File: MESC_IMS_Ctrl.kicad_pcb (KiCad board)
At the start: 4 copper layers, 100 x 75 mm, 187 parts, among them J1 Conn_01x08_Female, J10 Conn_01x04_Male, J2 Conn_01x08_Female, J3 Conn_01x08_Female, J4 Conn_01x06_Male, J5 Conn_ARM_JTAG_SWD_10, J6 USB_C_Receptacle_USB2.0, J7 Conn_01x03_Male, J8 Conn_01x04_Male, J9 Conn_01x08_Male, U1 STM32F303CBTx, U2 LM5017MR, U3 TPS76333, U4 INA240A1PW, U5 UCC21520DW, U6 INA240A1PW, U7 UCC21520DW, U8 INA240A1PW, U9 UCC21520DW, Y1 ASE-8.000MHZ-LC-T

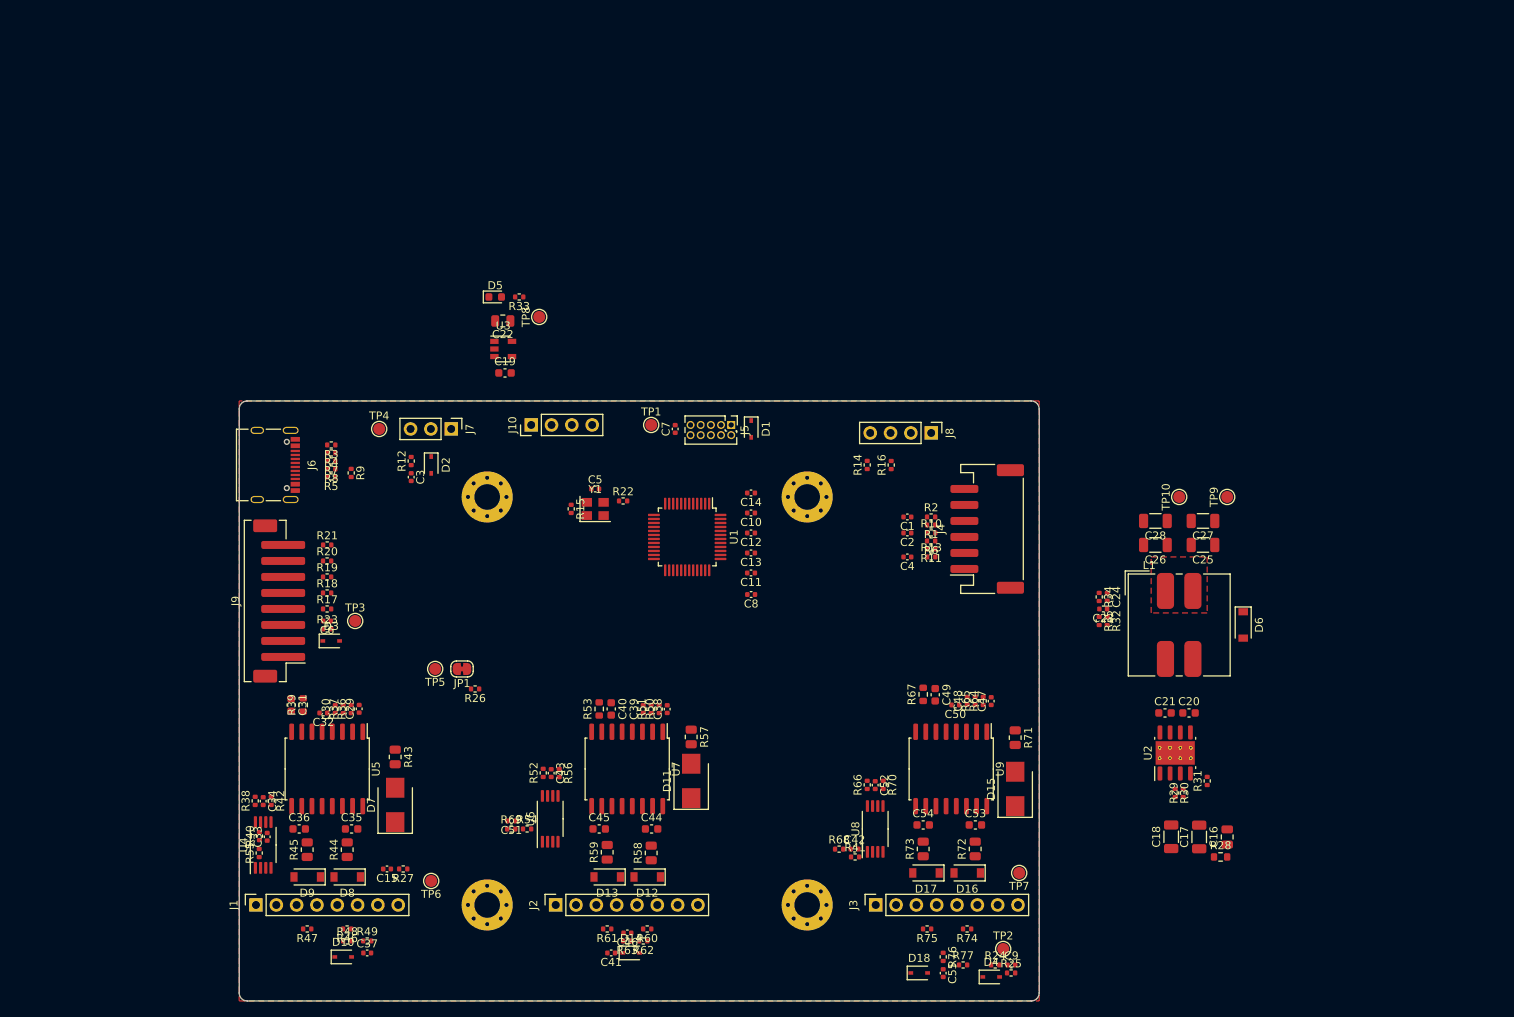
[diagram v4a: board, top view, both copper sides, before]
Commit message: Adding some basic test tracks
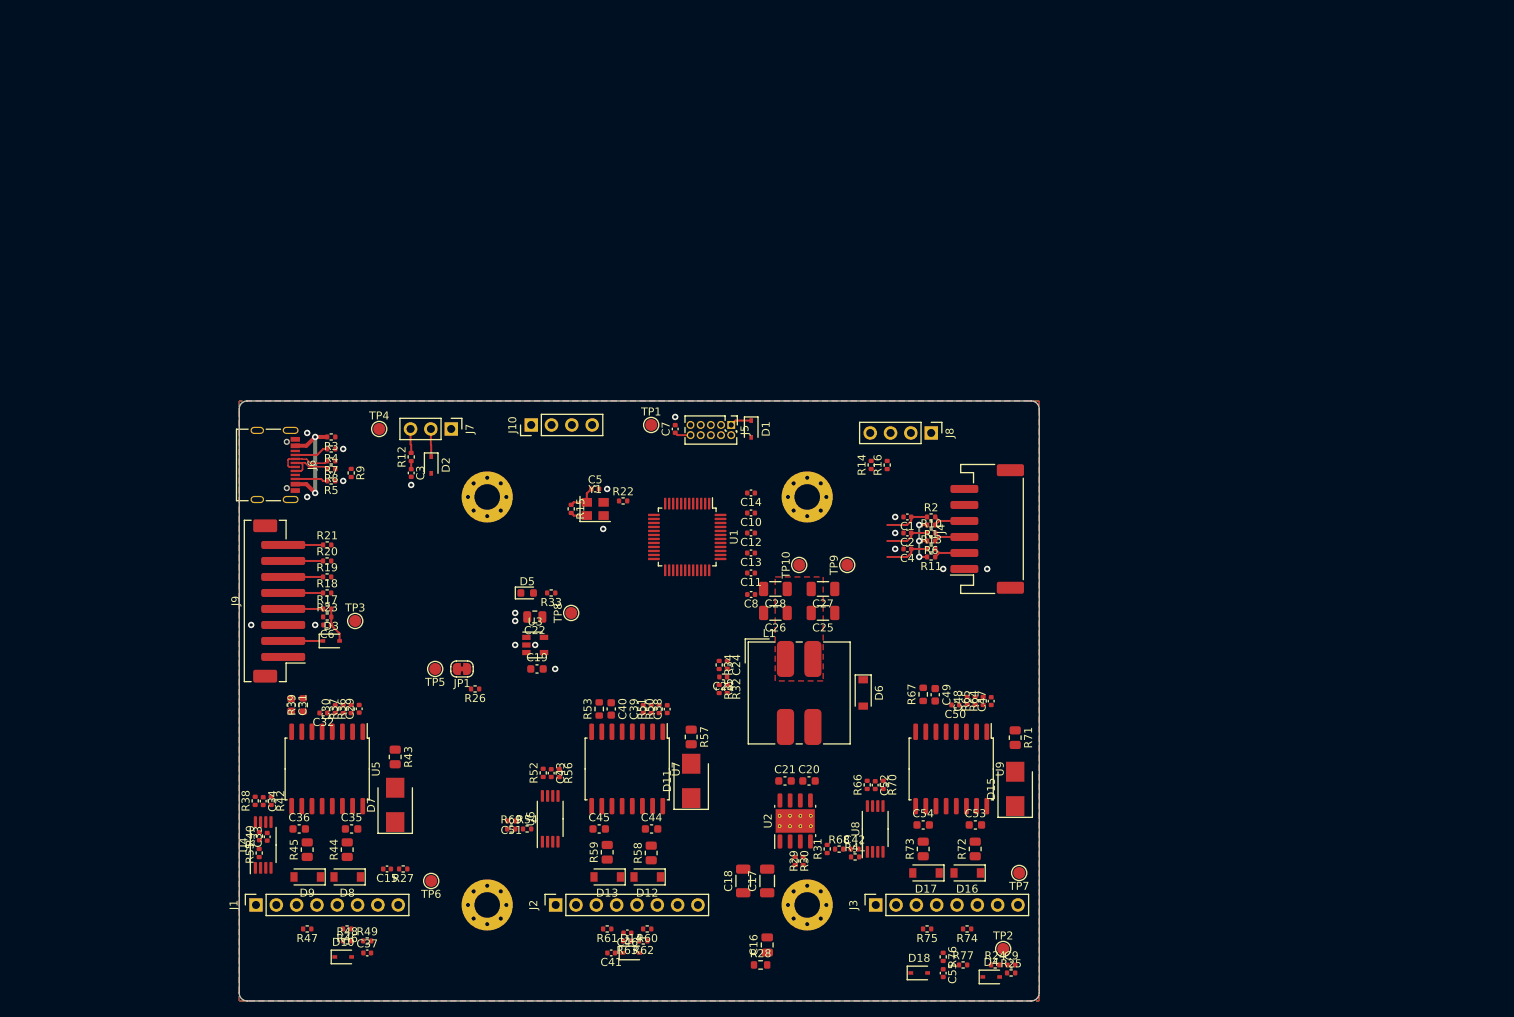
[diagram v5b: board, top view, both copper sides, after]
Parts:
- H1, H2, H3, H4: moved to F.Cu
- moved C16 59.1 mm to (175.0, 143.0)
- moved R28 59.1 mm to (174.2, 145.5)
- moved C17 54.3 mm to (175.0, 135.0)
- moved C18 53.8 mm to (172.0, 135.0)
- moved C20 48.3 mm to (180.2, 122.5)
- moved C21 48.3 mm to (177.2, 122.5)
- moved C23 48.3 mm to (169.5, 109.5)
- moved C24 48.3 mm to (170.0, 108.0)
- moved C25 48.3 mm to (182.0, 101.5)
- moved C26 48.3 mm to (176.0, 101.5)
- moved C27 48.3 mm to (182.0, 98.5)
- moved C28 48.3 mm to (176.0, 98.5)
- moved D6 48.3 mm to (187.0, 111.5)
- moved L1 48.3 mm to (179.0, 111.5)
- moved R29 48.3 mm to (179.5, 132.5)
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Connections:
- net Net-(J6-PadA6) renamed /D+
- net Net-(J6-PadA7) renamed /D-
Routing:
- net +3V3: track 0.00 -> 15.9 mm, vias 0 -> 3
- net Net-(J6-PadA4): track 0.00 -> 14.4 mm, vias 0 -> 2
- net /D-: track 0.00 -> 6.98 mm
- net /D+: track 0.00 -> 6.19 mm
- net /HALL_3: track 0.00 -> 5.70 mm
- net /HALL_2: track 0.00 -> 5.70 mm
- net /HALL_1: track 0.00 -> 5.69 mm
- net Net-(J9-Pad8): track 0.00 -> 4.99 mm
- net Net-(J9-Pad4): track 0.00 -> 4.99 mm
- net Net-(J9-Pad7): track 0.00 -> 4.98 mm
- net Net-(J9-Pad6): track 0.00 -> 4.98 mm
- net Net-(J9-Pad5): track 0.00 -> 4.98 mm
- net Net-(J4-Pad4): track 0.00 -> 4.56 mm
- net Net-(J4-Pad3): track 0.00 -> 4.56 mm
- net Net-(J4-Pad2): track 0.00 -> 4.56 mm
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- added copper zone on B.Cu, net GND
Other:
- copper layers 4 -> 2

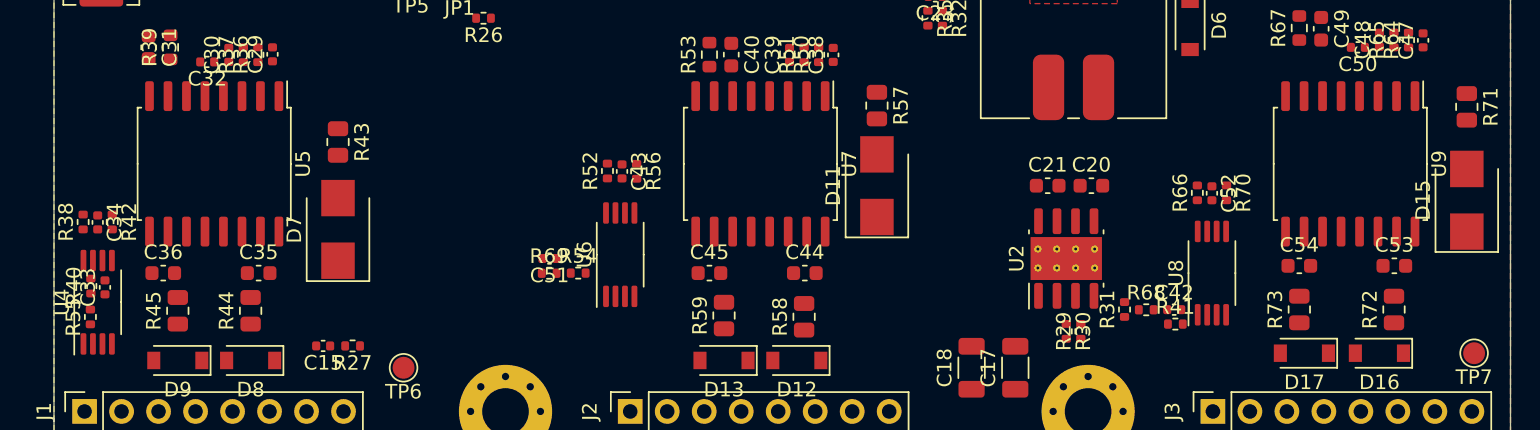
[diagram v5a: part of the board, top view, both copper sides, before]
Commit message: Cleaned up the schematic
Also regenerated the pdf & set boot diodes to SOD128.
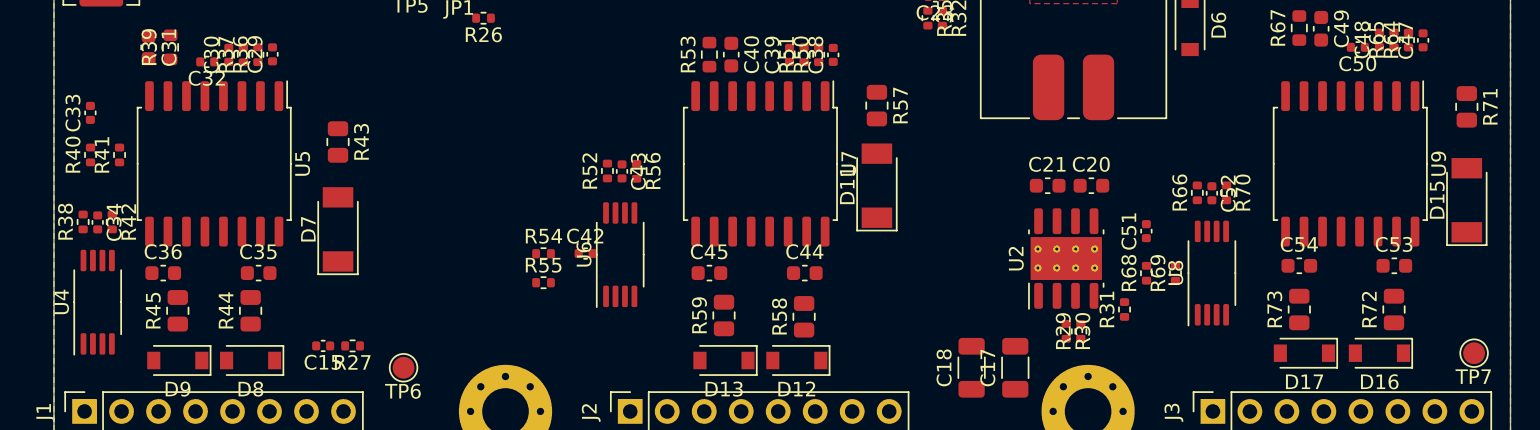
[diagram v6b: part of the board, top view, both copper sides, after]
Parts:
- removed svg2mod: G***, label
- D11, D15, D7: footprint Diode_SMD:D_SMB -> Diode_SMD:D_SOD-128
- R40, R54: value 150R -> 4k7
- R55, R69: value 4k7 -> 150R
- moved R41 73.4 mm to (113.5, 120.4), turned to 90 degrees
- moved R69 43.0 mm to (186.0, 128.5), turned to 90 degrees
- moved C51 41.0 mm to (184.0, 125.6), turned to 90 degrees
- moved C42 40.6 mm to (145.5, 127.2)
- moved R55 31.2 mm to (142.6, 129.2), turned to 0 degrees
- moved C33 12.0 mm to (111.5, 117.5)
- moved R40 9.00 mm to (111.5, 120.4)
- moved R54 2.73 mm to (142.6, 127.2)
- moved R68 2.51 mm to (184.0, 128.5), turned to 90 degrees
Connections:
- net /Phase_U/curr_sen- renamed /Phase_U/CURR_SEN-
- net /Phase_V/curr_sen- renamed /Phase_V/CURR_SEN-
- net /Phase_W/curr_sen- renamed /Phase_W/CURR_SEN-
- C42 pad 1: /ISW_MCU -> /ISV_MCU
- C51 pad 1: /ISV_MCU -> /ISW_MCU
- J1 pad 2: /ISU -> /Phase_U/CURR_SEN+
- J2 pad 2: /ISV -> /Phase_V/CURR_SEN+
- J3 pad 2: /ISW -> /Phase_W/CURR_SEN+
- R40 pad 1: /ISU_MCU -> +3V3
- R40 pad 2: /ISU -> /ISU_MCU
- R41 pad 1: /ISW_MCU -> /ISU_MCU
- R41 pad 2: /ISW -> /Phase_U/CURR_SEN+
- R54 pad 1: /ISV_MCU -> +3V3
- R54 pad 2: /ISV -> /ISV_MCU
- R55 pad 1: +3V3 -> /ISV_MCU
- R55 pad 2: /ISU_MCU -> /Phase_V/CURR_SEN+
- R69 pad 1: +3V3 -> /ISW_MCU
- R69 pad 2: /ISV_MCU -> /Phase_W/CURR_SEN+
- U4 pad 2: /ISU -> /Phase_U/CURR_SEN+
- U6 pad 2: /ISV -> /Phase_V/CURR_SEN+
- U8 pad 2: /ISW -> /Phase_W/CURR_SEN+

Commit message: Initial gate driver placement/routing
Also adding images to README
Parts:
- moved C41 26.5 mm to (159.0, 117.8)
- moved C12 16.3 mm to (157.0, 95.0)
- moved C8 16.0 mm to (168.0, 84.0), turned to 90 degrees
- moved C10 10.3 mm to (164.0, 84.0), turned to 90 degrees
- moved C11 8.75 mm to (173.0, 87.8), turned to 0 degrees
- moved R57 7.85 mm to (164.2, 124.8), turned to 90 degrees
- moved C13 7.78 mm to (168.0, 100.0), turned to 270 degrees
- moved C38 7.00 mm to (162.8, 106.5)
- moved C39 7.00 mm to (159.8, 106.5)
- moved R50 7.00 mm to (161.8, 106.5)
- moved R51 7.00 mm to (160.8, 106.5)
- moved D11 5.22 mm to (167.0, 127.5)
- moved U7 4.01 mm to (157.8, 125.0)
- moved C40 3.78 mm to (156.0, 117.2)
- moved R53 3.78 mm to (154.5, 117.2)
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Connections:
- net /SWO renamed Net-(J5-Pad6)
- net Net-(R22-Pad2) renamed /CLK
- U7 pad 7: Net-(U7-Pad7) -> GND
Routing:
- net +3V3: track 15.9 -> 105.2 mm, vias 3 -> 16
- net /USB_D+: track 0.00 -> 57.2 mm
- net /USB_D-: track 0.00 -> 56.4 mm
- net +5V: track 0.00 -> 51.1 mm, vias 0 -> 3
- net /Phase_U/GATE_DIS: track 0.00 -> 32.4 mm, vias 0 -> 1
- net /Phase_V/CURR_SEN+: track 0.00 -> 22.8 mm
- net /Phase_W/CURR_SEN+: track 0.00 -> 22.7 mm
- net VDD: track 0.00 -> 21.2 mm, vias 0 -> 2
- net /Phase_V/CURR_SEN-: track 0.00 -> 17.9 mm
- net /Phase_W/CURR_SEN-: track 0.00 -> 17.9 mm
- net /Phase_V/G_MID: track 0.00 -> 17.7 mm
- net /Phase_V/G_BOT: track 0.00 -> 13.2 mm
- net Net-(C38-Pad1): track 0.00 -> 11.8 mm
- net /ST_Tx: track 0.00 -> 11.8 mm
- net /Phase_U/CURR_SEN+: track 0.00 -> 11.7 mm, vias 0 -> 1
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
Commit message: Continuing routing
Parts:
- TP1, TP10, TP2, TP3, TP4, TP5, TP6, TP7, TP8, TP9: moved to B.Cu
- moved J10 30.3 mm to (175.8, 79.0)
- moved TP5 17.1 mm to (135.5, 125.5), turned to 90 degrees
- moved TP4 13.8 mm to (140.2, 80.0)
- moved JP1 13.7 mm to (135.5, 122.2), turned to 270 degrees
- moved R15 12.8 mm to (155.3, 76.5), turned to 180 degrees
- moved R26 9.52 mm to (138.0, 120.5), turned to 270 degrees
- moved C10 9.50 mm to (154.5, 84.0)
- moved C12 9.50 mm to (147.5, 95.0)
- moved C13 9.50 mm to (158.5, 100.0)
- moved C8 9.50 mm to (158.5, 84.0)
- moved U1 9.50 mm to (155.5, 92.0)
- moved C11 9.48 mm to (163.5, 88.0)
- moved C14 9.48 mm to (163.5, 89.0)
- moved Y1 9.41 mm to (155.2, 79.2), turned to 270 degrees
- moved C19 8.73 mm to (138.2, 112.0)
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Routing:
- net +3V3: track 105.2 -> 200.4 mm, vias 16 -> 21
- net /PWM_IN: track 1.01 -> 51.1 mm, vias 0 -> 3
- net /I2C_SCL: track 0.00 -> 42.5 mm, vias 0 -> 2
- net VDD: track 21.2 -> 63.0 mm, vias 2 -> 6
- net /I2C_SDA: track 0.00 -> 41.0 mm, vias 0 -> 1
- net /Phase_U/GATE_DIS: track 32.4 -> 68.0 mm, vias 1 -> 3
- net /ANA_IN: track 9.53 -> 42.7 mm, vias 0 -> 5
- net /HALL_3: track 11.8 -> 38.0 mm, vias 0 -> 2
- net /CAN_RX: track 0.00 -> 26.0 mm
- net /HALL_1: track 11.8 -> 37.6 mm, vias 0 -> 2
- net /HALL_2: track 11.8 -> 36.8 mm
- net /CAN_TX: track 0.00 -> 23.3 mm
- net /ST_Tx: track 11.8 -> 34.5 mm, vias 0 -> 2
- net /SWD_DIO: track 0.00 -> 21.8 mm, vias 0 -> 2
- net /V_V_SEN: track 11.2 -> 33.0 mm, vias 0 -> 2
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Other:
- net class Default: via_dia 0.8 -> 0.6; via_drill 0.4 -> 0.3
- rule via_min_size: 0.4 -> 0.3
